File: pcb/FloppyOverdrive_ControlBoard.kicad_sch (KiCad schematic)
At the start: 46 parts, among them J1 174804-1, J2 Motor_Header, J3 Floppy_Bus, J4 Sensor_Header, J5 Heads_Header, J6 Step_Header, J7 PIC_ADC_Header, J8 FPGA_IO_Header, J9 HeadOut_Header, SW1 RST_Btn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

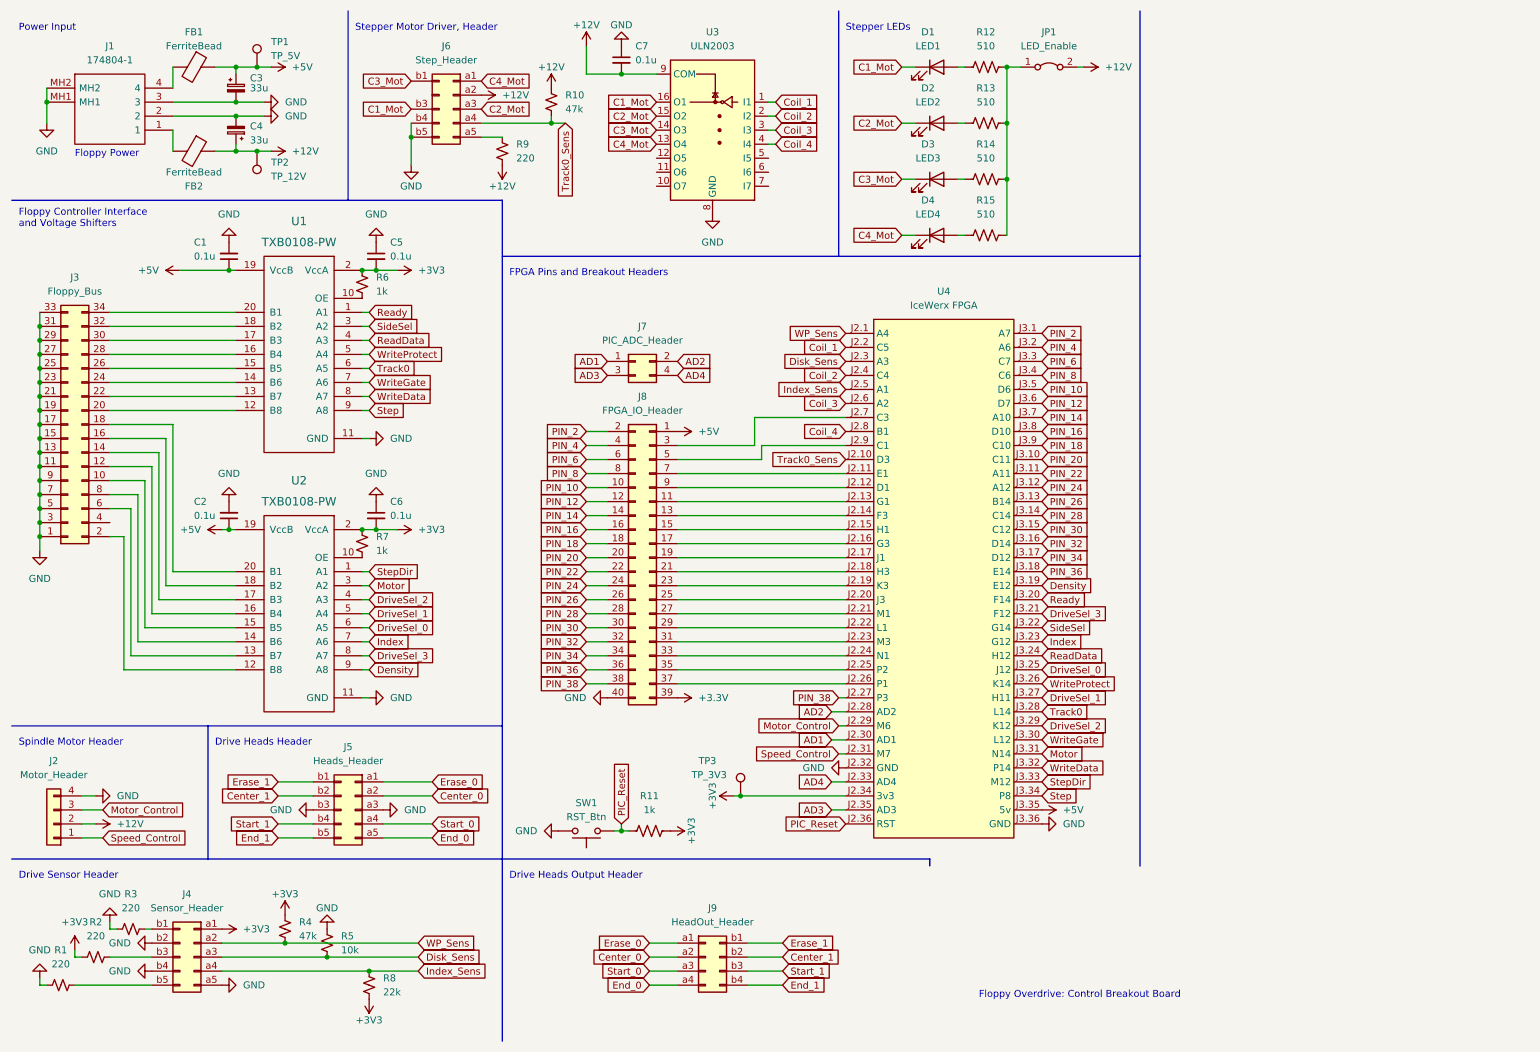
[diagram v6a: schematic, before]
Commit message: Added PCB test points, fixed schematic
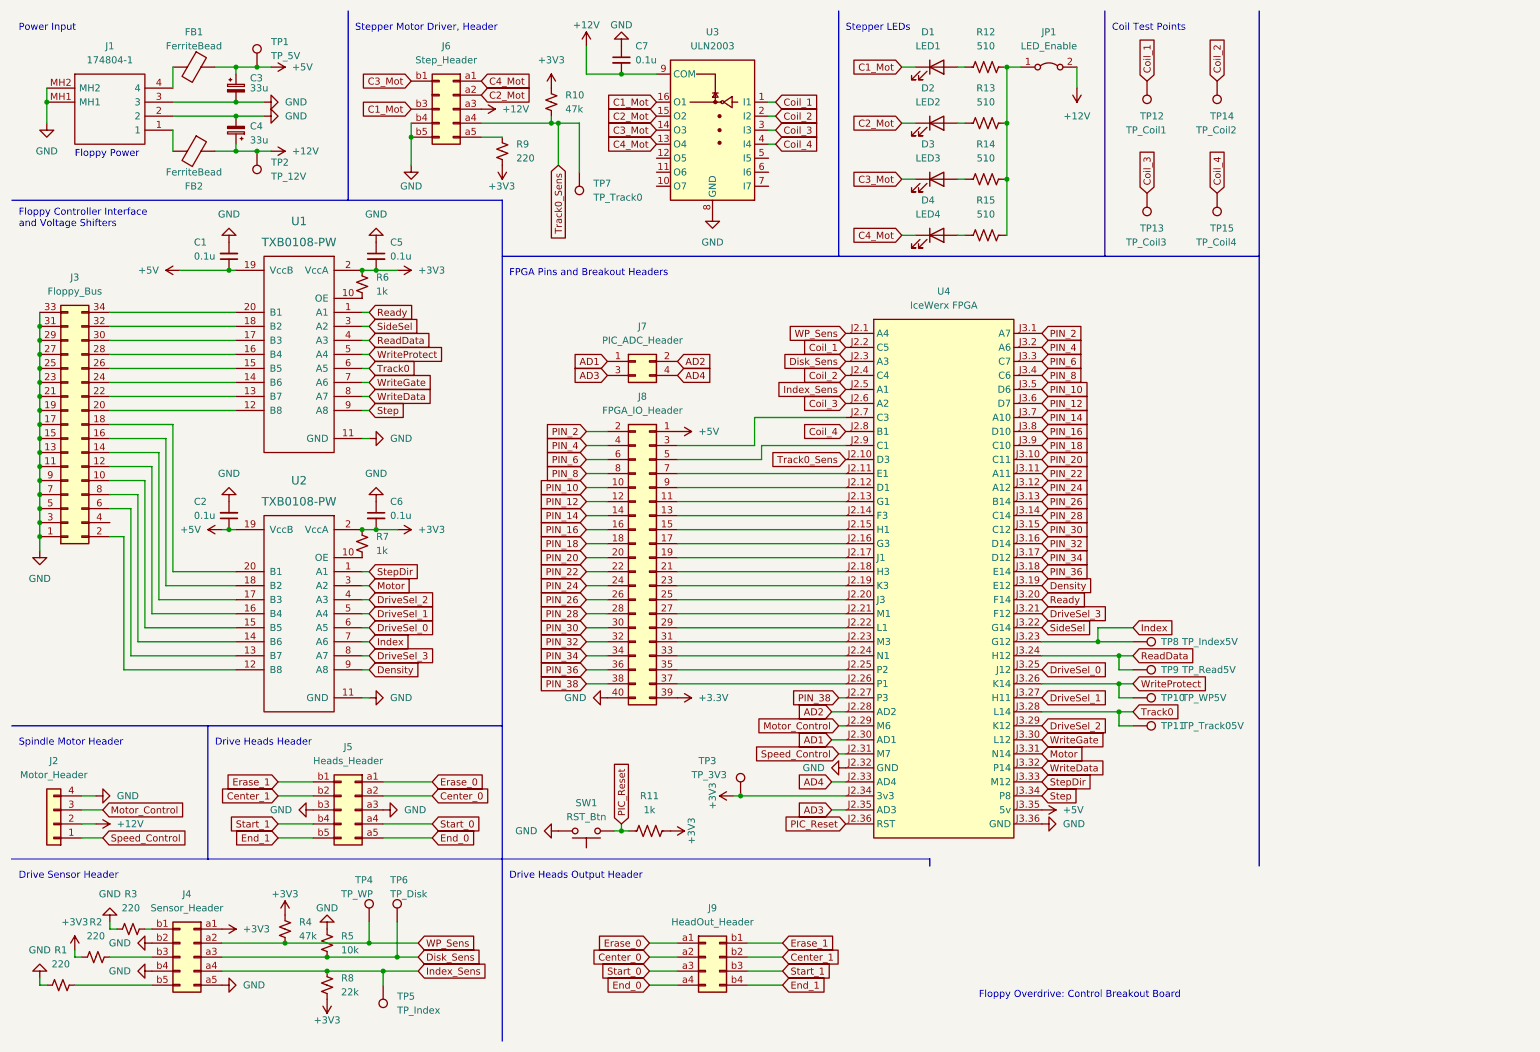
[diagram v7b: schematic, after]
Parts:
- added TP10: TP_WP5V, TestPoint:TestPoint_Pad_D1.0mm, symbol Connector:TestPoint
- added TP11: TP_Track05V, TestPoint:TestPoint_Pad_D1.0mm, symbol Connector:TestPoint
- added TP12: TP_Coil1, TestPoint:TestPoint_Pad_D1.0mm, symbol Connector:TestPoint
- added TP13: TP_Coil3, TestPoint:TestPoint_Pad_D1.0mm, symbol Connector:TestPoint
- added TP14: TP_Coil2, TestPoint:TestPoint_Pad_D1.0mm, symbol Connector:TestPoint
- added TP15: TP_Coil4, TestPoint:TestPoint_Pad_D1.0mm, symbol Connector:TestPoint
- added TP4: TP_WP, TestPoint:TestPoint_Pad_D1.0mm, symbol Connector:TestPoint
- added TP5: TP_Index, TestPoint:TestPoint_Pad_D1.0mm, symbol Connector:TestPoint
- added TP6: TP_Disk, TestPoint:TestPoint_Pad_D1.0mm, symbol Connector:TestPoint
- added TP7: TP_Track0, TestPoint:TestPoint_Pad_D1.0mm, symbol Connector:TestPoint
- added TP8: TP_Index5V, TestPoint:TestPoint_Pad_D1.0mm, symbol Connector:TestPoint
- added TP9: TP_Read5V, TestPoint:TestPoint_Pad_D1.0mm, symbol Connector:TestPoint
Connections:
- net +12V: now also J6.a3 (Pin_a3); no longer J6.a2 (Pin_a2), R10.1, R9.2
- net +3V3: now also R10.1, R9.2
- net C2_Mot: now also J6.a2 (Pin_a2); no longer J6.a3 (Pin_a3)
- net Coil_1: now also TP12.1
- net Coil_2: now also TP14.1
- net Coil_3: now also TP13.1
- net Coil_4: now also TP15.1
- net Disk_Sens: now also TP6.1
- net Index: now also TP8.1
- net Index_Sens: now also TP5.1
- net ReadData: now also TP9.1
- net Track0: now also TP11.1
- net Track0_Sens: now also TP7.1
- net WP_Sens: now also TP4.1
- net WriteProtect: now also TP10.1
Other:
- note added: "Coil Test Points"
- moved on the sheet: R8

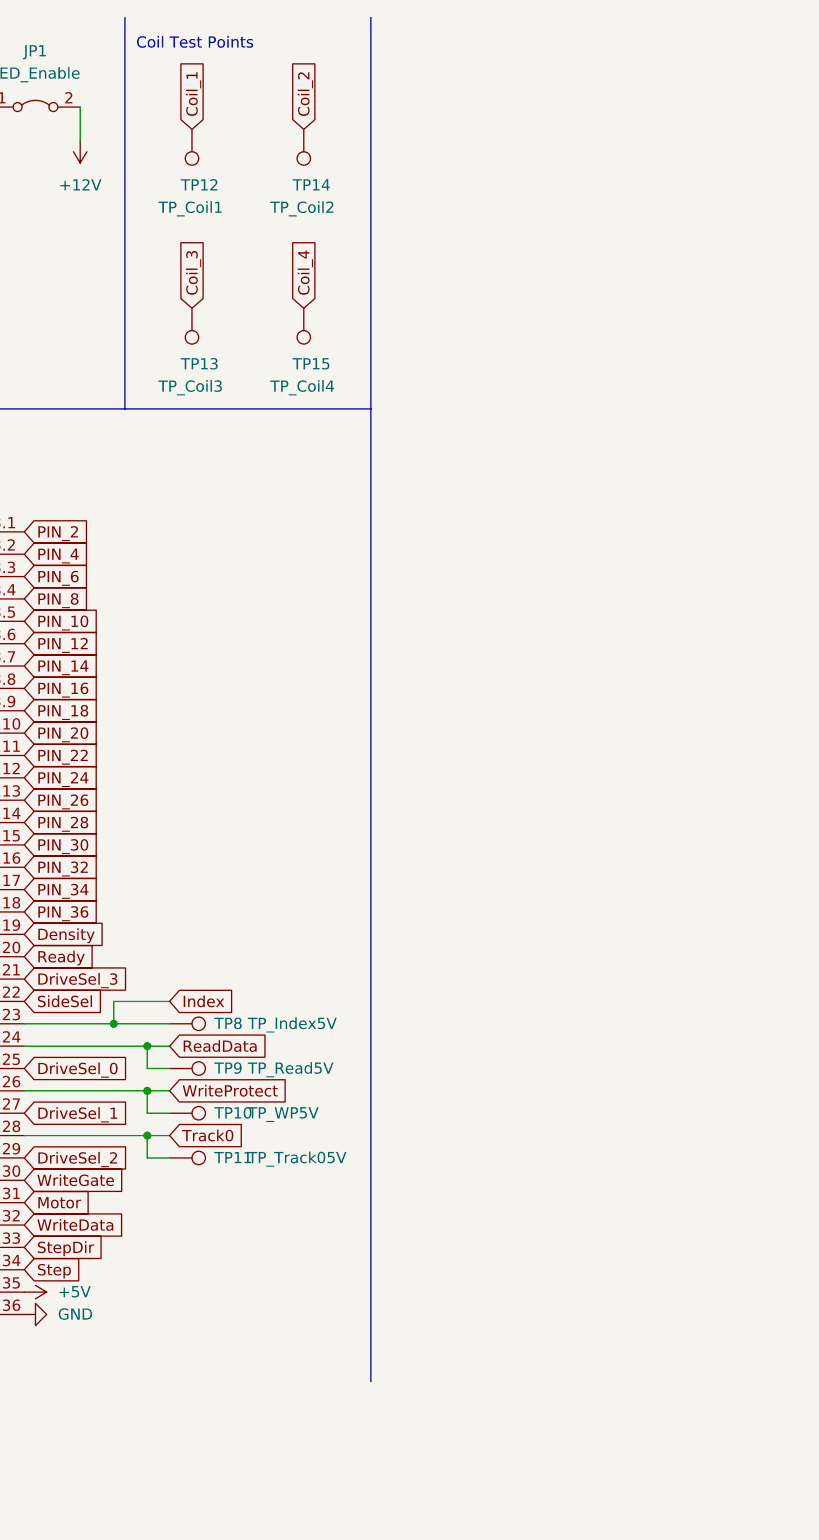
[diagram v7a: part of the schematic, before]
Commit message: Added neg voltage and amps
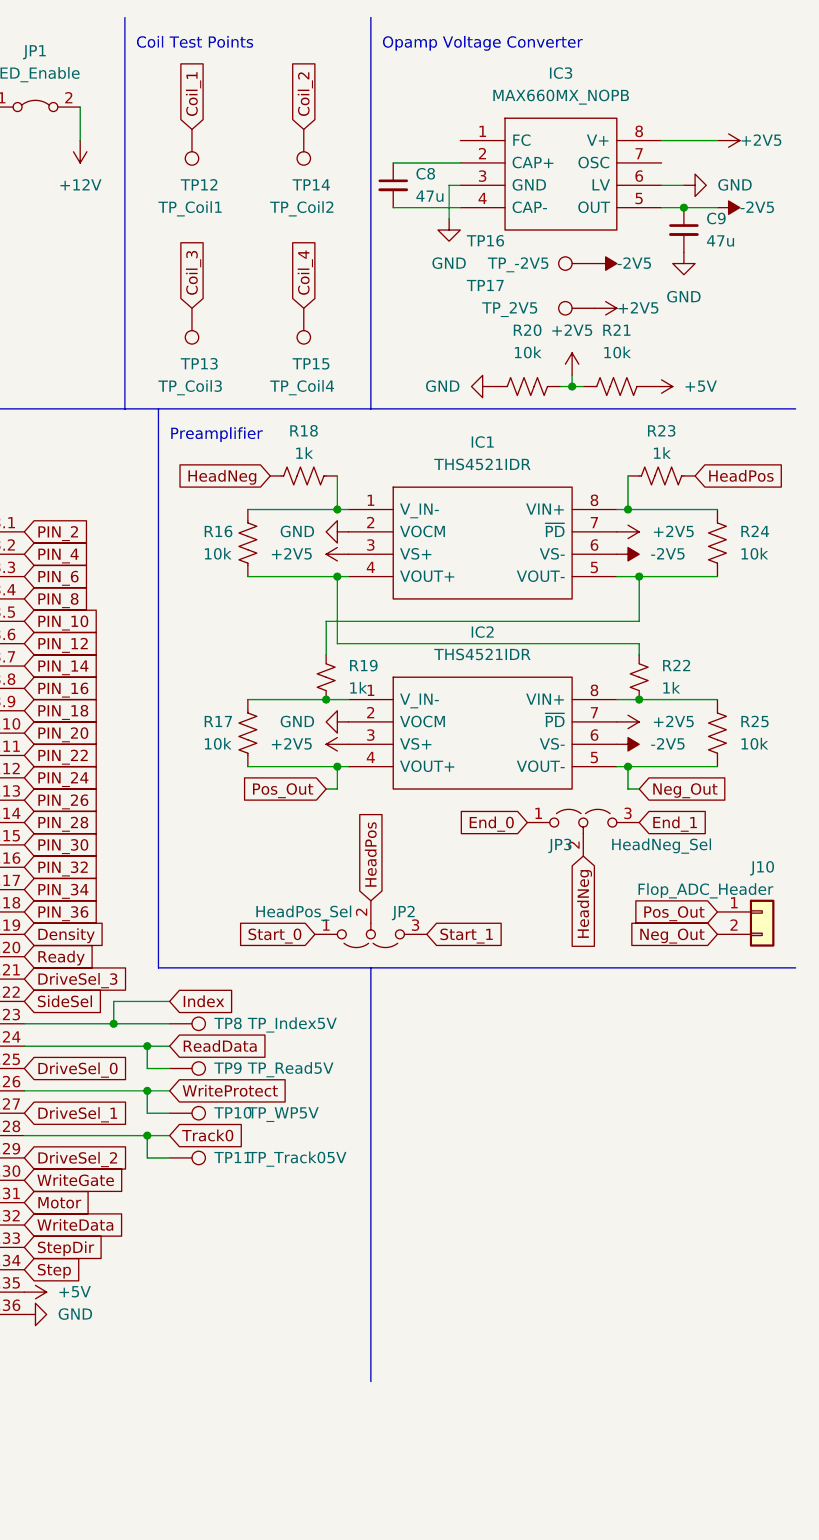
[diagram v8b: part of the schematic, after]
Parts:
- added C8, C9: 47u, Capacitor_THT:C_Disc_D5.0mm_W2.5mm_P2.50mm, symbol Device:C_Small
- added IC1, IC2: THS4521IDR, SOIC127P600X175-8N, symbol THS4521IDR:THS4521IDR
- added IC3: MAX660MX_NOPB, SOIC127P600X175-8N, symbol MAX660MX_NOPB:MAX660MX_NOPB
- added J10: Flop_ADC_Header, Connector_PinHeader_2.54mm:PinHeader_1x02_P2.54mm_Vertical, symbol Connector_Generic:Conn_01x02
- added JP2: HeadPos_Sel, Connector_PinHeader_2.54mm:PinHeader_1x03_P2.54mm_Vertical, symbol Jumper:Jumper_3_Open
- added JP3: HeadNeg_Sel, Connector_PinHeader_2.54mm:PinHeader_1x03_P2.54mm_Vertical, symbol Jumper:Jumper_3_Open
- added R16, R17, R20, R21, R24, R25: 10k, Resistor_SMD:R_0402_1005Metric, symbol Device:R_US
- added R18, R23: 1k, Resistor_SMD:R_0402_1005Metric, symbol Device:R_US
- added R19, R22: 1k, Resistor_SMD:R_0402_1005Metric, symbol Device:R_Small_US
- added TP16: TP_-2V5, TestPoint:TestPoint_Pad_D1.0mm, symbol Connector:TestPoint
- added TP17: TP_2V5, TestPoint:TestPoint_Pad_D1.0mm, symbol Connector:TestPoint
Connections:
- net +5V: now also R21.2
- net End_0: now also JP3.1 (A)
- net End_1: now also JP3.3 (B)
- net GND: now also C9.2, IC1.2 (VOCM), IC2.2 (VOCM), IC3.3 (GND), IC3.6 (LV), R20.1
- net Start_0: now also JP2.1 (A)
- net Start_1: now also JP2.3 (B)
- new net: IC1.5 (VOUT-), R19.1, R24.2
- new net: IC2.1 (V_IN-), R17.1, R19.2
- new net: IC1.1 (V_IN-), R16.1, R18.2
- new net: IC1.4 (VOUT+), R16.2, R22.1
- new net: IC2.8 (VIN+), R22.2, R25.1
- new net: IC1.8 (VIN+), R23.1, R24.1
- new net: C8.1, IC3.2 (CAP+)
- new net: C8.2, IC3.4 (CAP-)
- new net +2V5: IC1.3 (VS+), IC1.7 (~{PD}), IC2.3 (VS+), IC2.7 (~{PD}), IC3.8 (V+), R20.2, R21.1, TP17.1
- new net -2V5: C9.1, IC1.6 (VS-), IC2.6 (VS-), IC3.5 (OUT), TP16.1
- new net HeadNeg: JP3.2 (C), R18.1
- new net HeadPos: JP2.2 (C), R23.2
- new net Neg_Out: IC2.5 (VOUT-), J10.2 (Pin_2), R25.2
- new net Pos_Out: IC2.4 (VOUT+), J10.1 (Pin_1), R17.2
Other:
- note added: "Opamp Voltage Converter"
- note added: "Preamplifier"
